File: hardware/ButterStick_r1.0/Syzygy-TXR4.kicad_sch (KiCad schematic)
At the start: 19 parts, among them J5 SYZYGY-TXR-4, U15 TLV62569DRL

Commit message: hw.r1d0: Review complete, gerbers generated
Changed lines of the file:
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@@
   (title_block
     (title "ButterStick")
-    (date "2020-07-16")
+    (date "2020-07-17")
     (rev "r1.0")
     (company "GsD")
@@
   (junction (at 137.16 39.37) (diameter 0) (color 0 0 0 0))
   (junction (at 176.53 142.24) (diameter 0) (color 0 0 0 0))
+  (no_connect (at 180.34 139.7))
   (no_connect (at 213.36 139.7))
-  (no_connect (at 180.34 139.7))
   (bus_entry (at 161.29 96.52) (size 2.54 -2.54)
     (stroke (width 0.1524) (type solid) (color 0 0 0 0))
@@
     (stroke (width 0) (type solid) (color 0 0 0 0))
   )
-  (bus (pts (xy 165.1 101.6) (xy 165.1 104.14))
-    (stroke (width 0) (type solid) (color 0 0 0 0))
-  )
-  (bus (pts (xy 165.1 104.14) (xy 165.1 109.22))
-    (stroke (width 0) (type solid) (color 0 0 0 0))
-  )
-  (bus (pts (xy 165.1 109.22) (xy 165.1 114.3))
-    (stroke (width 0) (type solid) (color 0 0 0 0))
-  )
-  (bus (pts (xy 165.1 114.3) (xy 165.1 119.38))
-    (stroke (width 0) (type solid) (color 0 0 0 0))
-  )
-  (bus (pts (xy 165.1 119.38) (xy 165.1 121.92))
+  (bus (pts (xy 165.1 101.6) (xy 165.1 106.68))
+    (stroke (width 0) (type solid) (color 0 0 0 0))
+  )
+  (bus (pts (xy 165.1 106.68) (xy 165.1 111.76))
+    (stroke (width 0) (type solid) (color 0 0 0 0))
+  )
+  (bus (pts (xy 165.1 111.76) (xy 165.1 116.84))
+    (stroke (width 0) (type solid) (color 0 0 0 0))
+  )
+  (bus (pts (xy 165.1 116.84) (xy 165.1 121.92))
     (stroke (width 0) (type solid) (color 0 0 0 0))
   )
@@
     (stroke (width 0) (type solid) (color 0 0 0 0))
   )
-  (bus (pts (xy 165.1 127) (xy 165.1 129.54))
-    (stroke (width 0) (type solid) (color 0 0 0 0))
-  )
-  (bus (pts (xy 165.1 129.54) (xy 165.1 134.62))
-    (stroke (width 0) (type solid) (color 0 0 0 0))
-  )
-  (bus (pts (xy 165.1 134.62) (xy 165.1 139.7))
-    (stroke (width 0) (type solid) (color 0 0 0 0))
-  )
-  (bus (pts (xy 165.1 139.7) (xy 165.1 153.67))
+  (bus (pts (xy 165.1 127) (xy 165.1 132.08))
+    (stroke (width 0) (type solid) (color 0 0 0 0))
+  )
+  (bus (pts (xy 165.1 132.08) (xy 165.1 137.16))
+    (stroke (width 0) (type solid) (color 0 0 0 0))
+  )
+  (bus (pts (xy 165.1 137.16) (xy 165.1 147.32))
+    (stroke (width 0) (type solid) (color 0 0 0 0))
+  )
+  (bus (pts (xy 165.1 147.32) (xy 165.1 153.67))
     (stroke (width 0) (type solid) (color 0 0 0 0))
   )
@@
     (stroke (width 0) (type solid) (color 0 0 0 0))
   )
-  (bus (pts (xy 228.6 127) (xy 228.6 132.08))
-    (stroke (width 0) (type solid) (color 0 0 0 0))
-  )
-  (bus (pts (xy 228.6 132.08) (xy 228.6 137.16))
-    (stroke (width 0) (type solid) (color 0 0 0 0))
-  )
+  (bus (pts (xy 228.6 127) (xy 228.6 129.54))
+    (stroke (width 0) (type solid) (color 0 0 0 0))
+  )
+  (bus (pts (xy 228.6 129.54) (xy 228.6 134.62))
+    (stroke (width 0) (type solid) (color 0 0 0 0))
+  )
+  (bus (pts (xy 228.6 134.62) (xy 228.6 137.16))
+    (stroke (width 0) (type solid) (color 0 0 0 0))
+  )

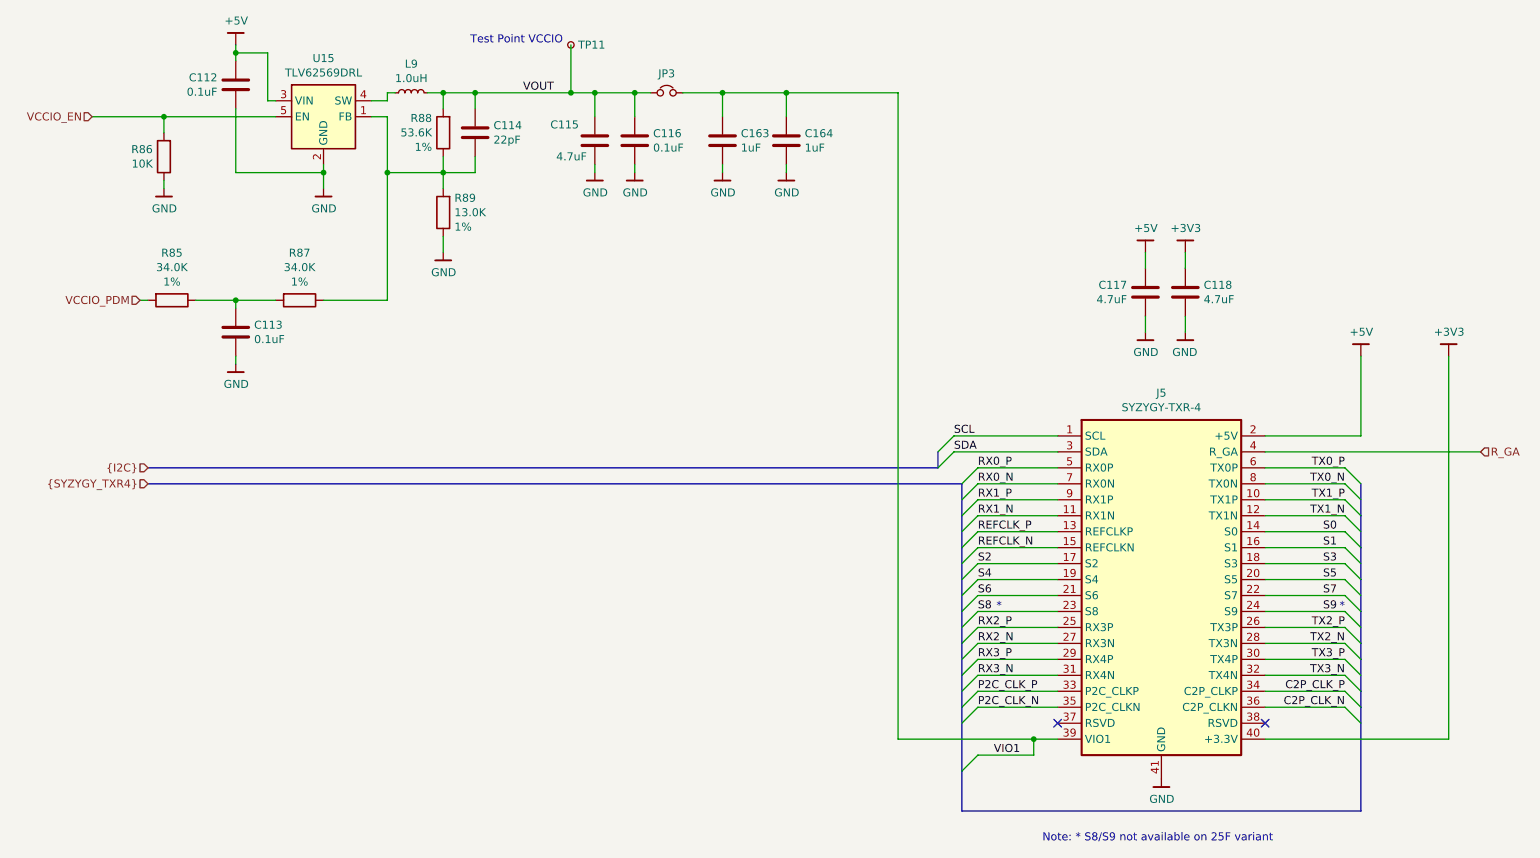
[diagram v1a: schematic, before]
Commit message: hw.r1d0: Update BOM fieids in schematic.
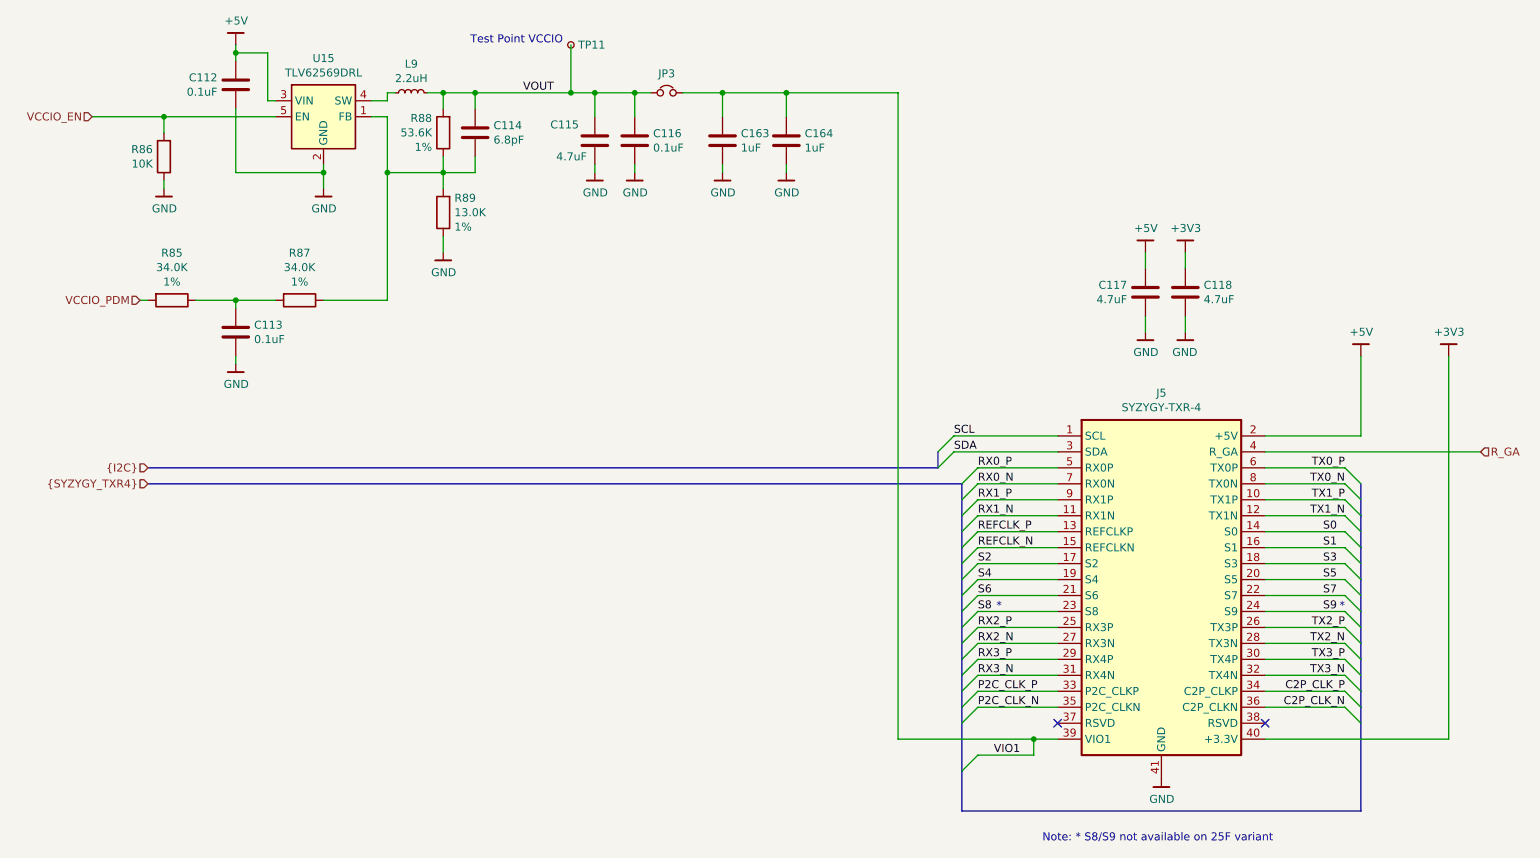
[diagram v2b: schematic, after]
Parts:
- C112, C116: Mfg Samsung Electro-Mechanics -> Yageo; PN CL05B104KP5NNNC -> CC0402KRX5R6BB104; Tol (none) -> 10V / X5R
- C113: Mfg Samsung Electro-Mechanics -> Yageo; PN (none) -> CC0402KRX5R6BB104; Tol (none) -> 10V / X5R
- C114: value 22pF -> 6.8pF; Mfg Samsung Electro-Mechanics -> Yageo; PN CL05B104KP5NNNC -> CC0402CRNPO9BN6R8
- C115, C117, C118: Mfg Samsung Electro-Mechanics -> Yageo; PN CL10A475KP8NNNC -> CC0603ZRY5V6BB475
- C163, C164: Mfg Samsung Electro-Mechanics -> Yageo; PN CL05B104KP5NNNC -> CC0402KRX5R6BB105
- J5: Mfg (none) -> Samtec Inc.; PN (none) -> QSH-020-01-F-D-DP-A
- L9: value 1.0uH -> 2.2uH; Mfg (none) -> Sunltech Tech; PN (none) -> SLM20122R2MIT
- R85, R87: Mfg Stackpole Electronics Inc -> Yageo; PN RNCF0402DTE10K0 -> RC0402FR-0734KL
- R86: Mfg Stackpole Electronics Inc -> Yageo; PN (none) -> RC0402FR-0710KL; Tol 1% -> (none)
- R88: Mfg Stackpole Electronics Inc -> Yageo; PN (none) -> RC0402FR-0753K6L
- R89: Mfg Stackpole Electronics Inc -> Yageo; PN (none) -> RC0402FR-0713KL
- TP11: PN (none) -> DNP
- U15: Mfg (none) -> Texas Instruments; PN (none) -> TLV62569DRLR
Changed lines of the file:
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@@
 (kicad_sch (version 20200618) (host eeschema "5.99.0-unknown-73168a9~101~ubuntu18.04.1")
-  (page 18 18)
+  (page 1 18)
   (paper "A4")
   (title_block
@@
     (stroke (width 0) (type solid) (color 0 0 0 0))
   )
-  (bus (pts (xy 165.1 121.92) (xy 165.1 127))
-    (stroke (width 0) (type solid) (color 0 0 0 0))
-  )
-  (bus (pts (xy 165.1 127) (xy 165.1 132.08))
+  (bus (pts (xy 165.1 121.92) (xy 165.1 124.46))
+    (stroke (width 0) (type solid) (color 0 0 0 0))
+  )
+  (bus (pts (xy 165.1 124.46) (xy 165.1 129.54))
+    (stroke (width 0) (type solid) (color 0 0 0 0))
+  )
+  (bus (pts (xy 165.1 129.54) (xy 165.1 132.08))
     (stroke (width 0) (type solid) (color 0 0 0 0))
   )
@@
       (effects (font (size 1.27 1.27)) hide)
     )
+    (property "PN" "DNP" (id 4) (at 102.87 31.75 0)
+      (effects (font (size 1.27 1.27)) hide)
+    )
   )
   (symbol (lib_id "Device:L_Small") (at 77.47 39.37 90) (unit 1)
     (in_bom yes) (on_board yes)
     (property "Reference" "L9" (id 0) (at 77.47 34.7788 90))
-    (property "Value" "1.0uH" (id 1) (at 77.47 37.0775 90))
+    (property "Value" "2.2uH" (id 1) (at 77.47 37.0775 90))
     (property "Footprint" "Inductor_SMD:L_0805_2012Metric" (id 2) (at 77.47 39.37 0)
       (effects (font (size 1.27 1.27)) hide)
     )
     (property "Datasheet" "~" (id 3) (at 77.47 39.37 0)
+      (effects (font (size 1.27 1.27)) hide)
+    )
+    (property "Mfg" "Sunltech Tech" (id 4) (at 77.47 39.37 0)
+      (effects (font (size 1.27 1.27)) hide)
+    )
+    (property "PN" "SLM20122R2MIT" (id 5) (at 77.47 39.37 0)
       (effects (font (size 1.27 1.27)) hide)
     )
@@
       (effects (font (size 1.27 1.27)) hide)
     )
-    (property "PN" "" (id 4) (at 38.1 49.53 0)
-      (effects (font (size 1.27 1.27)) hide)
-    )
-    (property "Mfg" "Stackpole Electronics Inc" (id 5) (at 38.1 49.53 0)
-      (effects (font (size 1.27 1.27)) hide)
-    )
-    (property "Tol" "1%" (id 6) (at 39.878 51.8414 0)
+    (property "PN" "RC0402FR-0710KL" (id 4) (at 38.1 49.53 0)
+      (effects (font (size 1.27 1.27)) hide)
+    )
+    (property "Mfg" "Yageo" (id 5) (at 38.1 49.53 0)
+      (effects (font (size 1.27 1.27)) hide)
+    )
+    (property "Tol" "" (id 6) (at 39.878 51.8414 0)
       (effects (font (size 1.27 1.27)) (justify right) hide)
     )
@@
       (effects (font (size 1.27 1.27)) hide)
     )
-    (property "PN" "RNCF0402DTE10K0" (id 4) (at 39.37 72.39 0)
-      (effects (font (size 1.27 1.27)) hide)
-    )
-    (property "Mfg" "Stackpole Electronics Inc" (id 5) (at 39.37 72.39 0)
+    (property "PN" "RC0402FR-0734KL" (id 4) (at 39.37 72.39 0)
+      (effects (font (size 1.27 1.27)) hide)
+    )
+    (property "Mfg" "Yageo" (id 5) (at 39.37 72.39 0)
       (effects (font (size 1.27 1.27)) hide)
     )
@@
       (effects (font (size 1.27 1.27)) hide)
     )
-    (property "PN" "RNCF0402DTE10K0" (id 4) (at 59.69 72.39 0)
-      (effects (font (size 1.27 1.27)) hide)
-    )
-    (property "Mfg" "Stackpole Electronics Inc" (id 5) (at 59.69 72.39 0)
+    (property "PN" "RC0402FR-0734KL" (id 4) (at 59.69 72.39 0)
+      (effects (font (size 1.27 1.27)) hide)
+    )
+    (property "Mfg" "Yageo" (id 5) (at 59.69 72.39 0)
       (effects (font (size 1.27 1.27)) hide)
     )
@@
       (effects (font (size 1.27 1.27)) hide)
     )
-    (property "PN" "" (id 4) (at 82.55 45.72 0)
-      (effects (font (size 1.27 1.27)) hide)
-    )
-    (property "Mfg" "Stackpole Electronics Inc" (id 5) (at 82.55 45.72 0)
+    (property "PN" "RC0402FR-0753K6L" (id 4) (at 82.55 45.72 0)
+      (effects (font (size 1.27 1.27)) hide)
+    )
+    (property "Mfg" "Yageo" (id 5) (at 82.55 45.72 0)
       (effects (font (size 1.27 1.27)) hide)
     )
@@
       (effects (font (size 1.27 1.27)) hide)
     )
-    (property "PN" "" (id 4) (at 82.55 58.42 0)
-      (effects (font (size 1.27 1.27)) hide)
-    )
-    (property "Mfg" "Stackpole Electronics Inc" (id 5) (at 82.55 58.42 0)
+    (property "PN" "RC0402FR-0713KL" (id 4) (at 82.55 58.42 0)
+      (effects (font (size 1.27 1.27)) hide)
+    )
+    (property "Mfg" "Yageo" (id 5) (at 82.55 58.42 0)
       (effects (font (size 1.27 1.27)) hide)
     )
@@
       (effects (font (size 1.27 1.27)) hide)
     )
-    (property "Mfg" "Samsung Electro-Mechanics" (id 4) (at 107.95 171.45 0)
-      (effects (font (size 1.27 1.27)) hide)
-    )
-    (property "PN" "CL05B104KP5NNNC" (id 5) (at 107.95 171.45 0)
+    (property "Mfg" "Yageo" (id 4) (at 107.95 171.45 0)
+      (effects (font (size 1.27 1.27)) hide)
+    )
+    (property "PN" "CC0402KRX5R6BB104" (id 5) (at 107.95 171.45 0)
+      (effects (font (size 1.27 1.27)) hide)
+    )
+    (property "Tol" "10V / X5R" (id 4) (at 49.53 38.1 0)
       (effects (font (size 1.27 1.27)) hide)
     )
@@
       (effects (font (size 1.27 1.27)) hide)
     )
-    (property "Mfg" "Samsung Electro-Mechanics" (id 4) (at -8.89 210.82 0)
-      (effects (font (size 1.27 1.27)) hide)
-    )
-    (property "PN" "" (id 5) (at -8.89 210.82 0)
+    (property "Mfg" "Yageo" (id 4) (at -8.89 210.82 0)
+      (effects (font (size 1.27 1.27)) hide)
+    )
+    (property "PN" "CC0402KRX5R6BB104" (id 5) (at -8.89 210.82 0)
+      (effects (font (size 1.27 1.27)) hide)
+    )
+    (property "Tol" "10V / X5R" (id 4) (at 49.53 77.47 0)
       (effects (font (size 1.27 1.27)) hide)
     )
@@
       (effects (font (size 1.27 1.27)) (justify left))
     )
-    (property "Value" "22pF" (id 1) (at 90.5511 46.8693 0)
+    (property "Value" "6.8pF" (id 1) (at 90.5511 46.8693 0)
       (effects (font (size 1.27 1.27)) (justify left))
     )
@@
       (effects (font (size 1.27 1.27)) hide)
     )
-    (property "Mfg" "Samsung Electro-Mechanics" (id 4) (at 29.21 179.07 0)
-      (effects (font (size 1.27 1.27)) hide)
-    )
-    (property "PN" "CL05B104KP5NNNC" (id 5) (at 29.21 179.07 0)
+    (property "Mfg" "Yageo" (id 4) (at 29.21 179.07 0)
+      (effects (font (size 1.27 1.27)) hide)
+    )
+    (property "PN" "CC0402CRNPO9BN6R8" (id 5) (at 29.21 179.07 0)
       (effects (font (size 1.27 1.27)) hide)
     )
@@
       (effects (font (size 1.27 1.27)) hide)
     )
-    (property "Mfg" "Samsung Electro-Mechanics" (id 4) (at -13.97 179.07 0)
-      (effects (font (size 1.27 1.27)) hide)
-    )
-    (property "PN" "CL10A475KP8NNNC" (id 5) (at -13.97 179.07 0)
+    (property "Mfg" "Yageo" (id 4) (at -13.97 179.07 0)
+      (effects (font (size 1.27 1.27)) hide)
+    )
+    (property "PN" "CC0603ZRY5V6BB475" (id 5) (at -13.97 179.07 0)
       (effects (font (size 1.27 1.27)) hide)
     )
@@
       (effects (font (size 1.27 1.27)) hide)
     )
-    (property "Mfg" "Samsung Electro-Mechanics" (id 4) (at 171.45 180.34 0)
-      (effects (font (size 1.27 1.27)) hide)
-    )
-    (property "PN" "CL05B104KP5NNNC" (id 5) (at 171.45 180.34 0)
+    (property "Mfg" "Yageo" (id 4) (at 171.45 180.34 0)
+      (effects (font (size 1.27 1.27)) hide)
+    )
+    (property "PN" "CC0402KRX5R6BB104" (id 5) (at 171.45 180.34 0)
+      (effects (font (size 1.27 1.27)) hide)
+    )
+    (property "Tol" "10V / X5R" (id 4) (at 113.03 46.99 0)
       (effects (font (size 1.27 1.27)) hide)
     )
@@
       (effects (font (size 1.27 1.27)) hide)
     )
-    (property "Mfg" "Samsung Electro-Mechanics" (id 4) (at 185.42 180.34 0)
-      (effects (font (size 1.27 1.27)) hide)
-    )
-    (property "PN" "CL05B104KP5NNNC" (id 5) (at 185.42 180.34 0)
+    (property "Mfg" "Yageo" (id 4) (at 185.42 180.34 0)
+      (effects (font (size 1.27 1.27)) hide)
+    )
+    (property "PN" "CC0402KRX5R6BB105" (id 5) (at 185.42 180.34 0)
       (effects (font (size 1.27 1.27)) hide)
     )
@@
       (effects (font (size 1.27 1.27)) hide)
     )
-    (property "Mfg" "Samsung Electro-Mechanics" (id 4) (at 195.58 180.34 0)
-      (effects (font (size 1.27 1.27)) hide)
-    )
-    (property "PN" "CL05B104KP5NNNC" (id 5) (at 195.58 180.34 0)
+    (property "Mfg" "Yageo" (id 4) (at 195.58 180.34 0)
+      (effects (font (size 1.27 1.27)) hide)
+    )
+    (property "PN" "CC0402KRX5R6BB105" (id 5) (at 195.58 180.34 0)
       (effects (font (size 1.27 1.27)) hide)
     )
@@
       (effects (font (size 1.27 1.27)) hide)
     )
-    (property "Mfg" "Samsung Electro-Mechanics" (id 4) (at 73.66 203.2 0)
-      (effects (font (size 1.27 1.27)) hide)
-    )
-    (property "PN" "CL10A475KP8NNNC" (id 5) (at 73.66 203.2 0)
+    (property "Mfg" "Yageo" (id 4) (at 73.66 203.2 0)
+      (effects (font (size 1.27 1.27)) hide)
+    )
+    (property "PN" "CC0603ZRY5V6BB475" (id 5) (at 73.66 203.2 0)
       (effects (font (size 1.27 1.27)) hide)
     )
@@
       (effects (font (size 1.27 1.27)) hide)
     )
-    (property "Mfg" "Samsung Electro-Mechanics" (id 4) (at 321.31 203.2 0)
-      (effects (font (size 1.27 1.27)) hide)
-    )
-    (property "PN" "CL10A475KP8NNNC" (id 5) (at 321.31 203.2 0)
+    (property "Mfg" "Yageo" (id 4) (at 321.31 203.2 0)
+      (effects (font (size 1.27 1.27)) hide)
+    )
+    (property "PN" "CC0603ZRY5V6BB475" (id 5) (at 321.31 203.2 0)
       (effects (font (size 1.27 1.27)) hide)
     )
@@
       (effects (font (size 1.27 1.27)) hide)
     )
+    (property "Mfg" "Texas Instruments" (id 4) (at 63.5 43.18 0)
+      (effects (font (size 1.27 1.27)) hide)
+    )
+    (property "PN" "TLV62569DRLR" (id 5) (at 63.5 43.18 0)
+      (effects (font (size 1.27 1.27)) hide)
+    )
   )
   (symbol (lib_id "gkl_misc:SYZYGY-TXR-4") (at 196.85 115.57 0) (unit 1)
@@
       (effects (font (size 1.27 1.27)) hide)
     )
+    (property "Mfg" "Samtec Inc." (id 4) (at 196.85 115.57 0)
+      (effects (font (size 1.27 1.27)) hide)
+    )
+    (property "PN" "QSH-020-01-F-D-DP-A" (id 5) (at 196.85 115.57 0)
+      (effects (font (size 1.27 1.27)) hide)
+    )
